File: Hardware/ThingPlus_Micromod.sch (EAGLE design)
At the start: 68 parts, among them J4 QWIIC_RIGHT_ANGLE, J5 MICRO-SD-SDIOPUSH-PUSH, J6 CORTEX_DEBUG, J7 MICROMOD-2222-C, U1 74LVC1G04SE, U2 MCP73831, U3 MAX17048, U4 3.3V, U5 3.3V

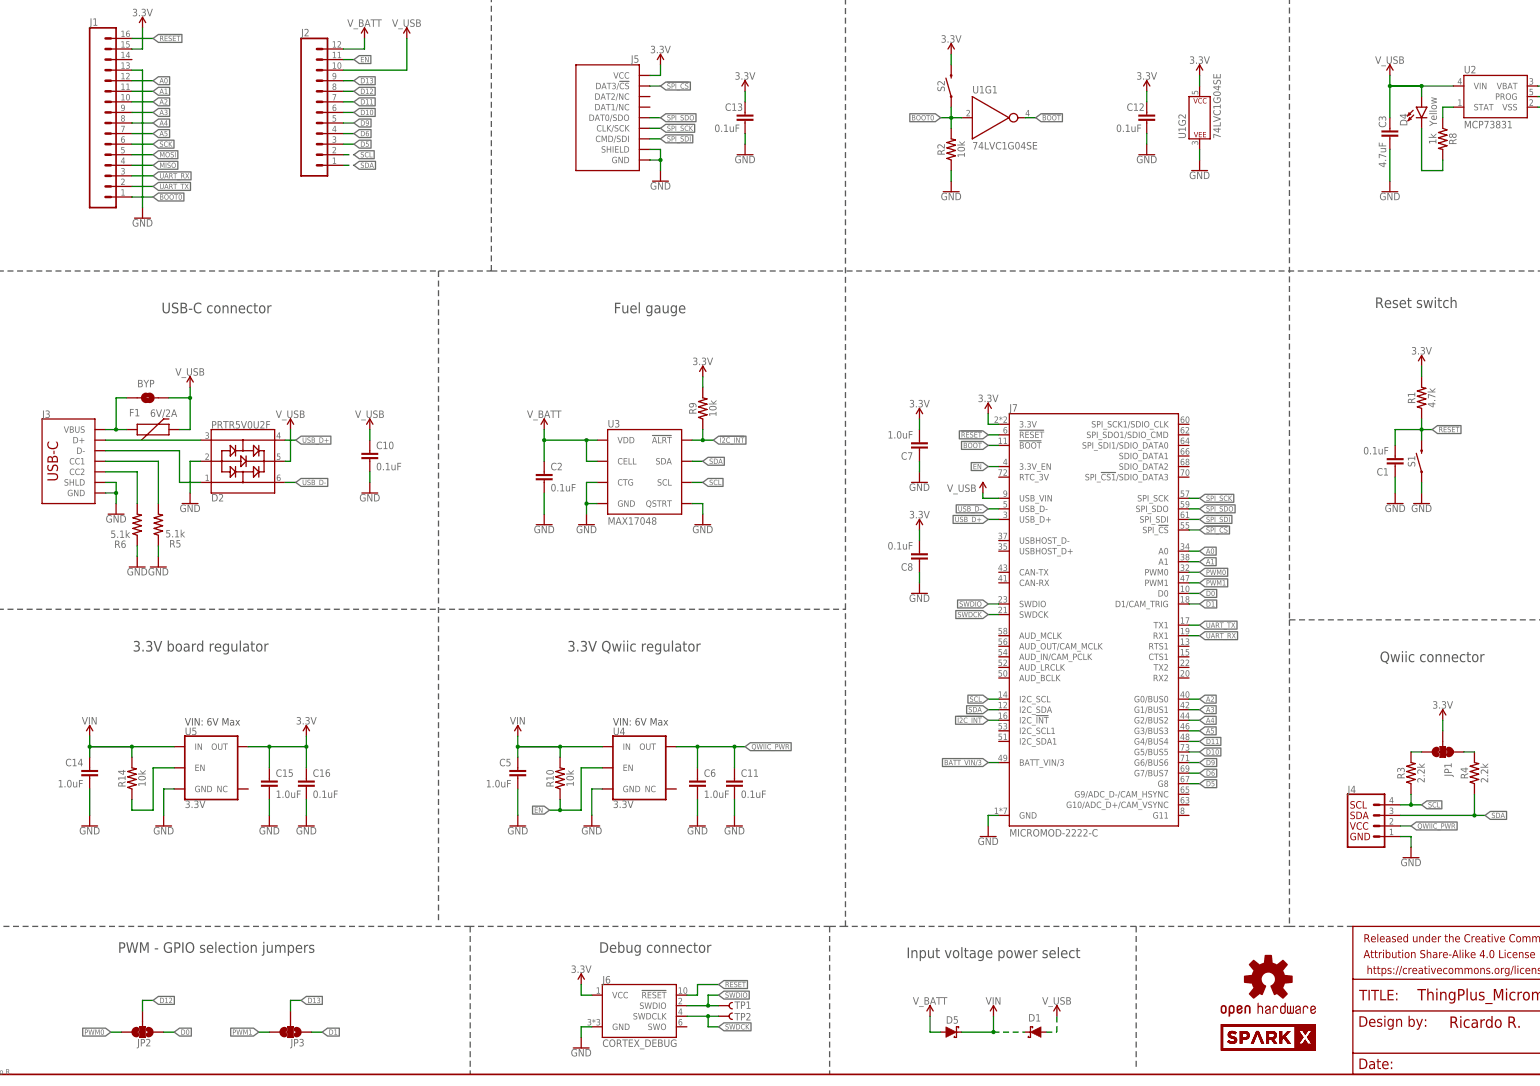
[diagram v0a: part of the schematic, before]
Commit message: Update SPI net names
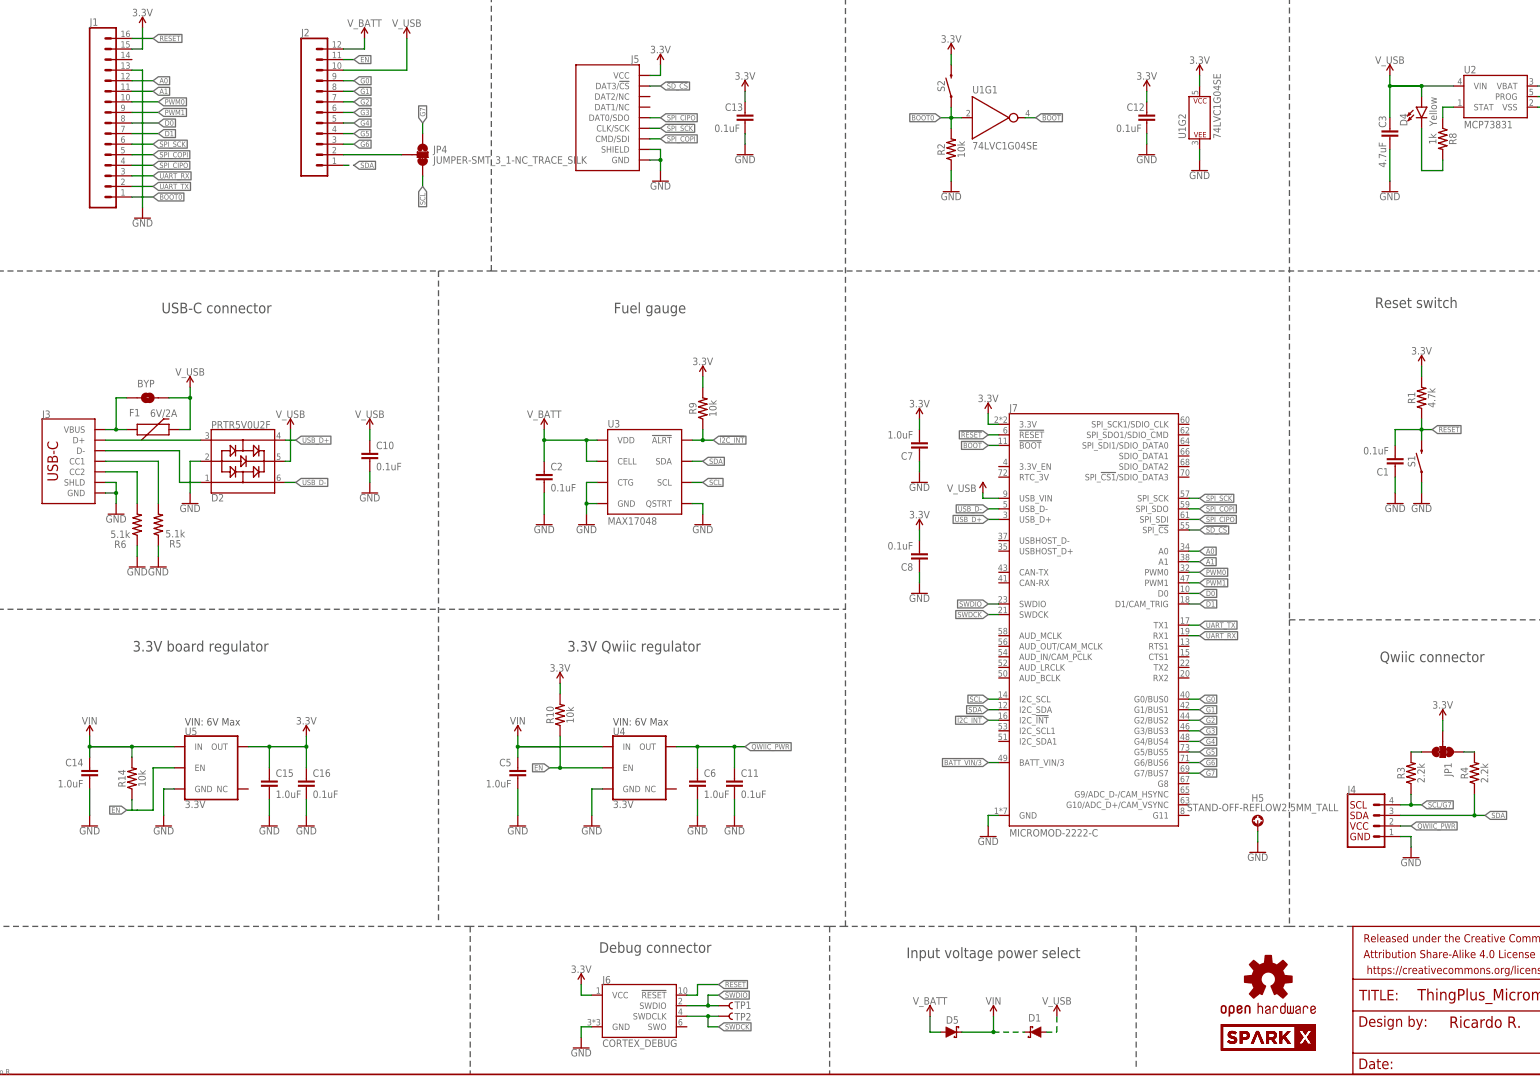
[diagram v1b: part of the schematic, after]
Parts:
- removed JP2, JP3: JUMPER-SMT_3_1-NC_TRACE_SILK, SparkFun-Jumpers:JUMPER-SMT_3_1-NC_TRACE_SILK
- added H5: STAND-OFF-REFLOW2.5MM_TALL, SparkFun-Hardware:STAND-OFF-REFLOW2.5MM_TALL
- added JP4: JUMPER-SMT_3_1-NC_TRACE_SILK, SparkFun-Jumpers:JUMPER-SMT_3_1-NC_TRACE_SILK
- H1, H2, H3, H4: value STAND-OFFTIGHT -> STAND-OFF; device SparkFun-Hardware:STAND-OFFTIGHT -> SparkFun-Hardware:STAND-OFF
- J3: device SparkFun-Connectors:USB_C_4-LAYER_PADS -> SparkFun-Connectors:USB_C_2-LAYER_PADS
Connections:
- net !SPI_CS! renamed !SD_CS!
- removed net A2: J1.10, J7.G0/BUS0
- removed net A3: J1.9, J7.G1/BUS1
- removed net A4: J1.8, J7.G2/BUS2
- removed net A5: J1.7, J7.G3/BUS3
- removed net D10: J2.6, J7.G5/BUS5
- removed net D11: J2.7, J7.G4/BUS4
- removed net D12: J2.8, JP2.2
- removed net D13: J2.9, JP3.2
- removed net D5: J2.3, J7.G8
- removed net D6: J2.4, J7.G7/BUS7
- removed net D9: J2.5, J7.G6/BUS6
- removed net MISO: J1.4
- removed net MOSI: J1.5
- removed net N$1: R14.1, U5.EN
- removed net SCK: J1.6
- removed net SPI_SDI: J5.CMD/SDI, J7.SPI_SDI
- removed net SPI_SDO: J5.DAT0/SDO, J7.SPI_SDO
- new net G0: J2.9, J7.G0/BUS0
- new net G1: J2.8, J7.G1/BUS1
- new net G2: J2.7, J7.G2/BUS2
- new net G3: J2.6, J7.G3/BUS3
- new net G4: J2.5, J7.G4/BUS4
- new net G5: J2.4, J7.G5/BUS5
- new net G6: J2.3, J7.G6/BUS6
- new net G7: J7.G7/BUS7, JP4.1
- new net N$5: J2.2, JP4.2
- new net SCL/G7: J4.4, R3.1
- new net SPI_CIPO: J1.4, J5.DAT0/SDO, J7.SPI_SDI
- new net SPI_COPI: J1.5, J5.CMD/SDI, J7.SPI_SDO
- net 3.3V: now also R10.2
- net D0: now also J1.8; no longer JP2.1
- net D1: now also J1.7; no longer JP3.1
- net EN: now also R14.1, U5.EN; no longer J7.3.3V_EN
- net GND: now also H5.1
- net PWM0: now also J1.10; no longer JP2.3
- net PWM1: now also J1.9; no longer JP3.3
- net SCL: now also JP4.3; no longer J2.2, J4.4, R3.1
- net SPI_SCK: now also J1.6
- net VIN: no longer R10.2
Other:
- note removed: "PWM - GPIO selection jumpers"
- moved on the sheet: R10

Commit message: Corrected schematic, board layout WIP
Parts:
- removed BYP: JUMPER-SMT_2_NO_SILK, SparkFun-Jumpers:JUMPER-SMT_2_NO_SILK
- removed C1, C12, C16, C9: 0.1uF, SparkFun-Capacitors:0.1UF-0603-25V-(+80/-20%)
- removed C14, C15: 1.0uF, SparkFun-Capacitors:1.0UF-0603-16V-10%
- removed D3: RED, SparkFun-LED:LED-RED0603
- removed F1: 6V/2A, SparkFun-Fuses:PPTC_6V2A
- removed FD1: FIDUCIALUFIDUCIAL, SparkFun-Aesthetics:FIDUCIALUFIDUCIAL
- removed PWR: JUMPER-SMT_2_NC_TRACE_NO-SILK, SparkFun-Jumpers:JUMPER-SMT_2_NC_TRACE_NO-SILK
- removed R11: 1k, SparkFun-Resistors:1KOHM-0402T-1/16W-1%
- removed R14: 10k, SparkFun-Resistors:10KOHM-0603-1/10W-1%
- removed R5: 5.1k, SparkFun-Resistors:5.1KOHM5.1KOHM-0603-1/10W-1%
- removed R8: 1k, SparkFun-Resistors:1KOHM-0603-1/10W-1%
- removed TP1, TP2: TEST-POINT3, SparkFun-Connectors:TEST-POINT3
- removed U1: 74LVC1G04SE, SparkFun-IC-Logic:74LVC1G04SE
- removed U5: 3.3V, SparkFun-IC-Power:V_REG_AP2112K-3.3V
- added 3V3_LED, VIN_LED: JUMPER-SMT_2_NC_TRACE_SILK, SparkFun-Jumpers:JUMPER-SMT_2_NC_TRACE_SILK
- added BYP1, VE: JUMPER-SMT_2_NO_SILK, SparkFun-Jumpers:JUMPER-SMT_2_NO_SILK
- added C17, C22: 0.22uF, SparkFun-Capacitors:0.22UF-0603-25V-10%
- added C18, C21: 0.1uF, SparkFun-Capacitors:0.1UF-0603-25V-(+80/-20%)
- added C19: 10uF, SparkFun-Capacitors:10UF-POLAR-EIA3216-16V-10%(TANT)
- added C20: 1.0uF, SparkFun-Capacitors:1.0UF-0603-16V-10%
- added D6: 3.3V, SparkFun-DiscreteSemi:DIODE-ZENER-MM3Z3V3T1G
- added D7: RED, SparkFun-LED:LED-RED0603
- added D8: Yellow, SparkFun-LED:LED-YELLOW0603
- added F2: 6V/2A, SparkFun-Fuses:PPTC_6V2A
- added MEAS, MEAS_BATT: JUMPER-COMBO_2_NC_TRACE, SparkFun-Jumpers:JUMPER-COMBO_2_NC_TRACE
- added R15: 100k, SparkFun-Resistors:100KOHM-0603-1/10W-1%
- added R16: 1k, SparkFun-Resistors:1KOHM-0603-1/10W-1%
- added R17: 4.7k, SparkFun-Resistors:4.7KOHM-0603-1/10W-1%
- added U6: AP7361C-33, SparkFun-IC-Power:AP7361C-33FGEUDFN-8
- C3: device SparkFun-Capacitors:4.7UF-0603-6.3V-(10%) -> SparkFun-Capacitors:4.7UF-0603-35V-(20%)
- C4: device SparkFun-Capacitors:4.7UF-0603-35V-(20%) -> SparkFun-Capacitors:4.7UF-0603-6.3V-(10%)
- D2: value PRTR5V0U2F -> Yellow; device SparkFun-IC-Power:PRTR5V0U2F -> SparkFun-LED:LED-YELLOW0603
- D4: value Yellow -> 3A/10V/280mV; device SparkFun-LED:LED-YELLOW0603 -> SparkFun-DiscreteSemi:DIODE-SCHOTTKY-BAT60A
- J6: value CORTEX_DEBUG -> JTAG; device SparkFun-Connectors:CORTEX_JTAG_DEBUG_MINIMUM_PTH_NS -> SparkFun-Connectors:CORTEX_JTAG_DEBUG_MINIMUM_PTH
- R1: value 4.7k -> 5.1k; device SparkFun-Resistors:4.7KOHM-0603-1/10W-1% -> SparkFun-Resistors:5.1KOHM5.1KOHM-0603-1/10W-1%
- R10: value 10k -> 100k; device SparkFun-Resistors:10KOHM-0603-1/10W-1% -> SparkFun-Resistors:100KOHM-0603-1/10W-1%
- R12: value 5.1k -> 20k; device SparkFun-Resistors:5.1KOHM5.1KOHM-0603-1/10W-1% -> SparkFun-Resistors:20KOHM-0603-1/10W-1%
- R13: value 9.76k -> 10k; device SparkFun-Resistors:9.76KOHM-0603-1/10W-1% -> SparkFun-Resistors:10KOHM-0603-1/10W-1%
- R2: value 10k -> 5.1k; device SparkFun-Resistors:10KOHM-0603-1/10W-1% -> SparkFun-Resistors:5.1KOHM5.1KOHM-0603-1/10W-1%
- R6: value 5.1k -> 2.2k; device SparkFun-Resistors:5.1KOHM5.1KOHM-0603-1/10W-1% -> SparkFun-Resistors:2.2KOHM-0603-1/10W-1%
- R7: value 2.0k -> 1k; device SparkFun-Resistors:2.0KOHM-0603-1/10W-5% -> SparkFun-Resistors:1KOHM-0603-1/10W-1%
- S1: value MOMENTARY-SWITCH-SPST-SMD-4.6X2.8MM -> Reset; device SparkFun-Switches:MOMENTARY-SWITCH-SPST-SMD-4.6X2.8MM -> SparkFun-Switches:MOMENTARY-SWITCH-SPST-SMD-5.2-TALL-REDUNDANT
- S2: value MOMENTARY-SWITCH-SPST-SMD-4.6X2.8MM -> BOOT; device SparkFun-Switches:MOMENTARY-SWITCH-SPST-SMD-4.6X2.8MM -> SparkFun-Switches:MOMENTARY-SWITCH-SPST-SMD-5.2-TALL-REDUNDANT
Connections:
- removed net !RESET: J6.!RESET
- removed net 5V_RAW: BYP.1, F1.1, J3.VBUS
- removed net CC1: J3.CC1, R5.2
- removed net CC2: J3.CC2, R6.2
- removed net D+_RAW: D2.3, J3.D+
- removed net D-_RAW: D2.1, J3.D-
- removed net N$15: R8.1, U2.STAT
- removed net N$2: PWR.1, R11.2
- removed net N$7: D3.A, R11.1
- new net 3.3V_EN: J7.3.3V_EN, VE.1
- new net 3.3V_EN_VE: D6.C, R15.1, U6.EN, VE.2
- new net 5V: C3.1, D2.A, D4.C, MEAS_BATT.1, U2.VIN
- new net CHG_LED: R7.1, U2.STAT
- new net N$1: MEAS.1, U6.OUT
- new net N$10: R17.2, VIN_LED.1
- new net N$11: D8.A, R17.1
- new net N$12: J3.CC1, R2.2
- new net N$13: J3.CC2, R1.2
- new net N$6: 3V3_LED.1, R16.2
- new net N$9: D7.A, R16.1
- net !BOOT!: now also S2.2; no longer U1G1.Y
- net !RESET!: now also J6.!RESET; no longer C1.2, R1.1
- net 3.3V: now also 3V3_LED.2, C20.1, C21.1, C22.1, MEAS.2; no longer C12.1, C15.1, C16.1, PWR.2, R1.2, S2.2, U1G2.P$V+, U5.OUT
- net BOOT0: no longer R2.2, S2.1, U1G1.A
- net EN: no longer R14.1, U5.EN
- net GND: now also C17.2, C18.2, C19.-, C20.2, C21.2, C22.2, D6.A, D7.C, D8.C, R1.1, S2.1, U6.GND; no longer C1.1, C12.2, C14.2, C15.2, C16.2, C9.2, D2.2, D3.C, J3.SHLD, R5.1, R7.1, U1G2.P$V-, U5.GND
- net N$14: now also D2.C, R7.2; no longer D4.C, R8.2
- net N$8: now also R6.2; no longer R7.2
- net SWDCK: no longer TP2.1
- net SWDIO: no longer TP1.1
- net USB_D+: now also J3.D+; no longer D2.4
- net USB_D-: now also J3.D-; no longer D2.6
- net VIN: now also BYP1.2, C17.1, C18.1, C19.+, F2.2, MEAS_BATT.2, R15.2, U6.IN, VIN_LED.2; no longer C14.1, R14.2, U5.IN
- net V_BATT: now also D4.A; no longer C9.1
- net V_USB: now also BYP1.1, F2.1, J3.VBUS; no longer BYP.2, C3.1, D2.5, D4.A, F1.2, U2.VIN
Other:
- note added: "Charge current: 450mA (1000V/Rprog)"
- note added: "Close VE to enable processor control of 3.3V bus."
- note added: "Closing jumper bypasses PTC to allow >2A current flows."
- note added: "LiPo Charger"
- note added: "LiPo Range: 3.6-4.2V"
- note added: "MicroMod connector"
- note added: "Open jumper to switch or measure power"
- note added: "SWO"
- note added: "USB"
- note added: "VIN: 3.7-6.0V"
- note added: "Voltage Regulation"
- note removed: "3.3V board regulator"
- note removed: "BATT_VIN/3 maximum voltage will be 3.28 V with 5V input"
- note removed: "BOOT0 switch and inverter"
- note removed: "Battery charger"
- note removed: "Debug connector"
- note removed: "Power LED"
- note removed: "Reset switch"
- note removed: "USB-C connector"
- moved on the sheet: C10, C11, C13, C2, C3, C4, C5, C6, C7, C8, D1, D5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

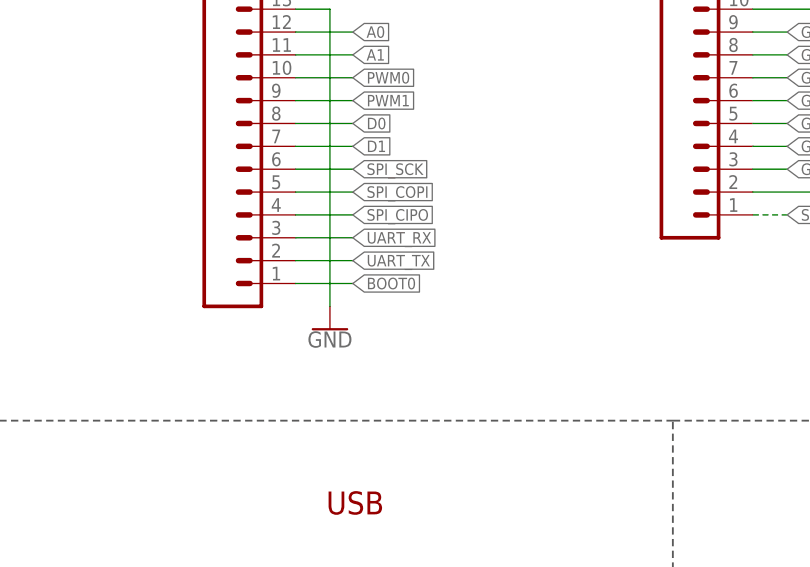
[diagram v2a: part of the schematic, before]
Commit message: ThingPlus Micromod board routing WIP
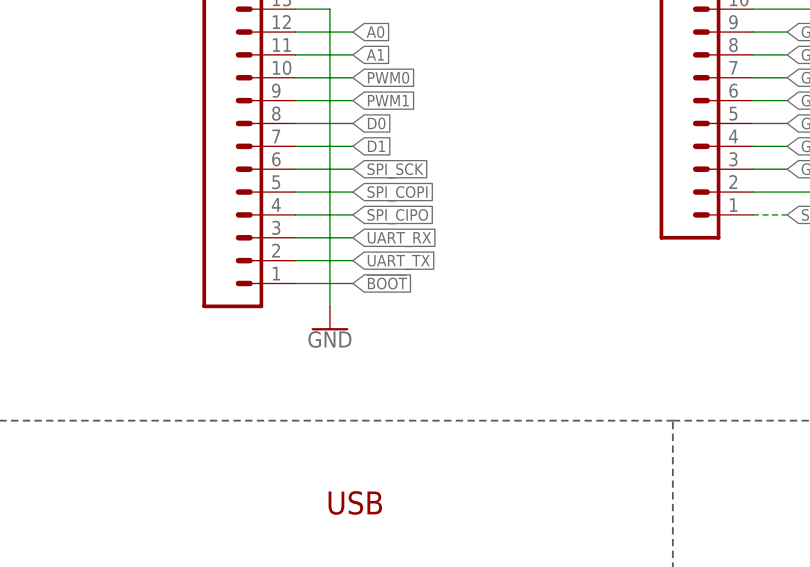
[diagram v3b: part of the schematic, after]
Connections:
- removed net BOOT0: J1.1
- net !BOOT!: now also J1.1
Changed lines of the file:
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@@
 <setting verticaltext="up"/>
 </settings>
-<grid distance="0.1" unitdist="inch" unit="mil" style="lines" multiple="1" display="yes" altdistance="0.01" altunitdist="inch" altunit="mil"/>
+<grid distance="0.1" unitdist="inch" unit="inch" style="lines" multiple="1" display="no" altdistance="0.01" altunitdist="inch" altunit="inch"/>
 <layers>
 <layer number="1" name="Top" color="4" fill="1" visible="no" active="no"/>
@@
 </segment>
 </net>
-<net name="BOOT0" class="0">
-<segment>
-<pinref part="J1" gate="G$1" pin="1"/>
-<wire x1="36.83" y1="210.82" x2="43.18" y2="210.82" width="0.1524" layer="91"/>
-<label x="43.18" y="210.82" size="1.27" layer="95" xref="yes"/>
-</segment>
-</net>
 <net name="SCL/G7" class="0">
 <segment>
@@
 </segment>
 </net>
-<net name="3.3V" class="1">
+<net name="3.3V" class="0">
 <segment>
 <pinref part="J1" gate="G$1" pin="15"/>
@@
 </segment>
 </net>
-<net name="V_USB" class="1">
+<net name="V_USB" class="0">
 <segment>
 <pinref part="J2" gate="G$1" pin="10"/>
@@
 <label x="383.54" y="116.84" size="1.27" layer="95" xref="yes"/>
 </segment>
-</net>
+<segment>
+<pinref part="J1" gate="G$1" pin="1"/>
+<wire x1="36.83" y1="210.82" x2="43.18" y2="210.82" width="0.1524" layer="91"/>
+<label x="43.18" y="210.82" size="1.27" layer="95" xref="yes"/>
+</segment>
+</net>

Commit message: Preliminary version of routed board.
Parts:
- added FD1: FIDUCIALUFIDUCIAL, SparkFun-Aesthetics:FIDUCIALUFIDUCIAL
- J3: device SparkFun-Connectors:USB_C_2-LAYER_PADS -> SparkFun-Connectors:USB_C_4-LAYER_PADS
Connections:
- net GND: now also J3.SHLD
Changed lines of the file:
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@@
 <part name="S1" library="SparkFun-Switches" deviceset="MOMENTARY-SWITCH-SPST" device="-SMD-5.2-TALL-REDUNDANT" value="Reset"/>
 <part name="GND5" library="SparkFun-PowerSymbols" deviceset="GND" device=""/>
-<part name="J3" library="SparkFun-Connectors" deviceset="USB_C" device="_2-LAYER_PADS"/>
+<part name="J3" library="SparkFun-Connectors" deviceset="USB_C" device="_4-LAYER_PADS"/>
 <part name="R2" library="SparkFun-Resistors" deviceset="5.1KOHM" device="5.1KOHM-0603-1/10W-1%" value="5.1k"/>
 <part name="R1" library="SparkFun-Resistors" deviceset="5.1KOHM" device="5.1KOHM-0603-1/10W-1%" value="5.1k"/>
@@
 <part name="S2" library="SparkFun-Switches" deviceset="MOMENTARY-SWITCH-SPST" device="-SMD-5.2-TALL-REDUNDANT" value="BOOT"/>
 <part name="GND15" library="SparkFun-PowerSymbols" deviceset="GND" device=""/>
+<part name="FD1" library="SparkFun-Aesthetics" deviceset="FIDUCIAL" device="UFIDUCIAL"/>
 </parts>
 <sheets>
@@
 <attribute name="VALUE" x="381" y="98.806" size="1.778" layer="96" rot="MR0" align="top-center"/>
 </instance>
+<instance part="FD1" gate="G$1" x="403.86" y="25.4" smashed="yes"/>
 </instances>
 <busses>
@@
 <wire x1="35.56" y1="152.4" x2="35.56" y2="149.86" width="0.1524" layer="91"/>
 <pinref part="GND10" gate="1" pin="GND"/>
-</segment>
-<segment>
+<pinref part="J3" gate="J1" pin="SHLD"/>
+<wire x1="33.02" y1="154.94" x2="35.56" y2="154.94" width="0.1524" layer="91"/>
+<wire x1="35.56" y1="154.94" x2="35.56" y2="152.4" width="0.1524" layer="91"/>
+<junction x="35.56" y="152.4"/>
+</segment>
+<segment>
